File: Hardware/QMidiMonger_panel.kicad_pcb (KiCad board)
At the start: 2 copper layers, 40.3 x 128.5 mm, 26 parts

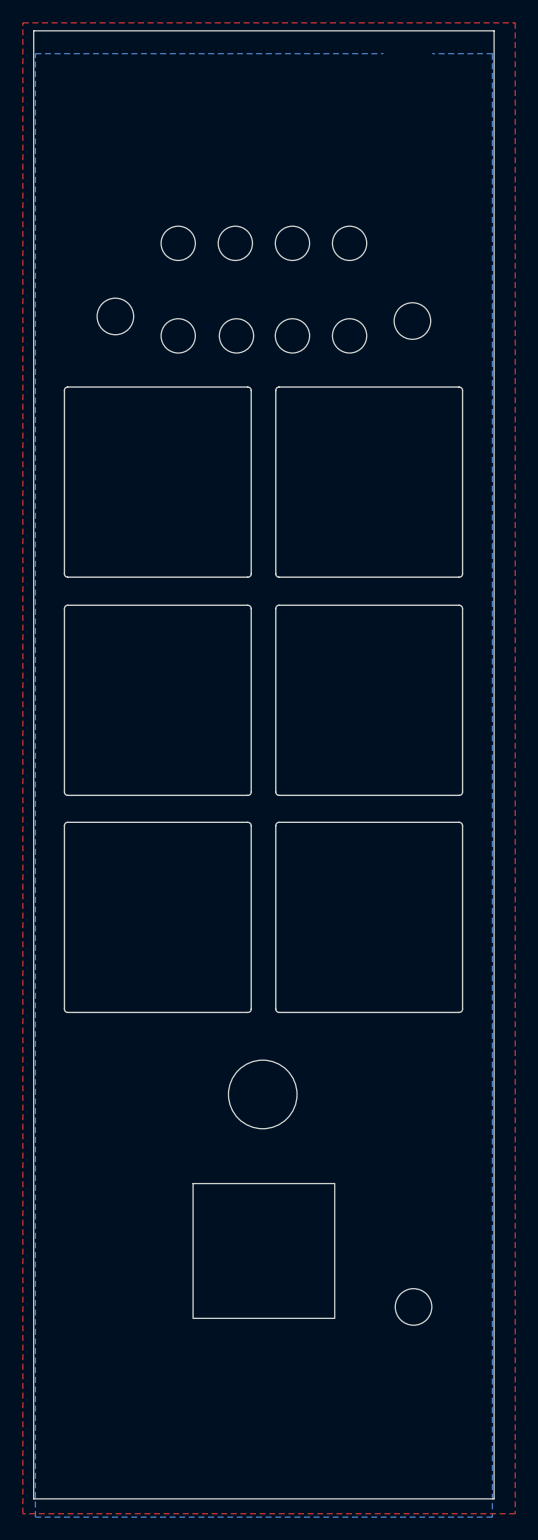
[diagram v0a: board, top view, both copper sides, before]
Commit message: Added inter-board connector
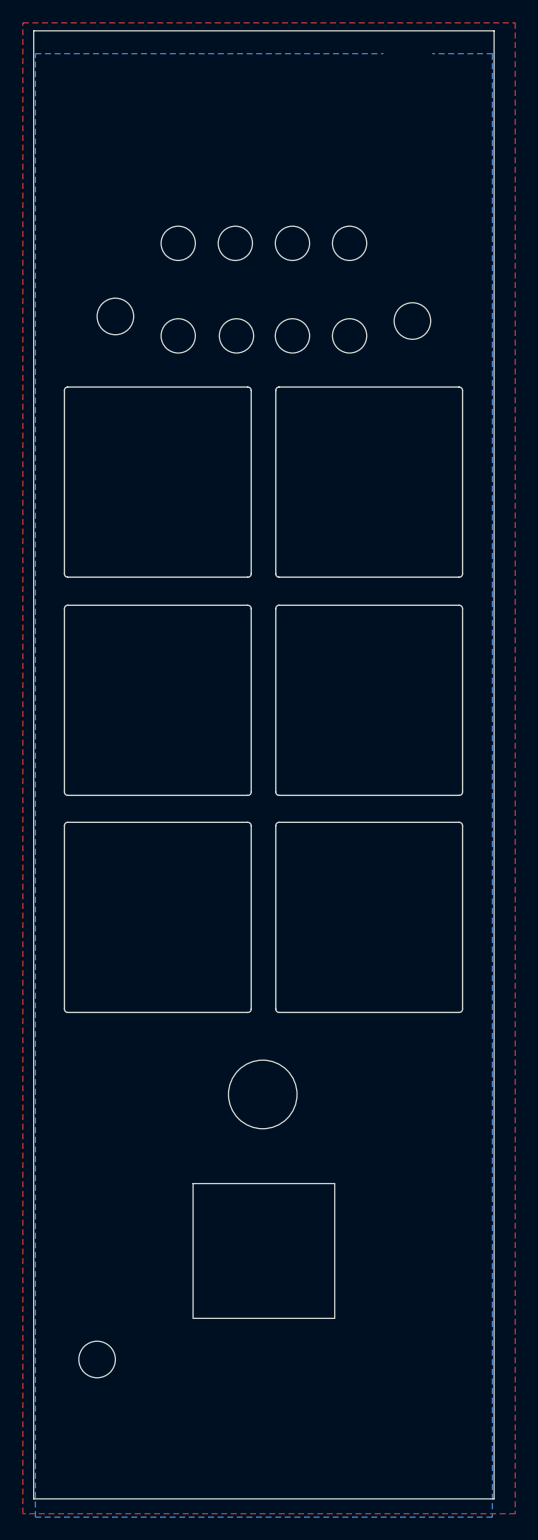
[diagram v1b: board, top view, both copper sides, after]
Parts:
- removed kibuzzard-63FE2BC1: G***, kibuzzard-63FE2BC1
- added kibuzzard-63FF48D8: G***, kibuzzard-63FF48D8, F.Cu at (116.0, 146.8)
- moved H3 28.1 mm to (101.4, 145.3)

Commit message: Cleaned up Panel and Controls
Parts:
- added H3: MountingHole, MountingHole:MountingHole_3.2mm_M3_ISO14580, F.Cu at (130.7, 142.4)
- moved H3 2.90 mm to (101.3, 142.4)
- moved Ref** 1.60 mm to (108.5, 54.1)
- moved Ref** 1.60 mm to (118.5, 54.1)
- moved Ref** 1.60 mm to (113.6, 54.1)
- moved Ref** 1.60 mm to (123.5, 54.1)
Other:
- board text added: "Mountjoy Modular 2023 Quad MIDI Monger Panel v1.0"
- board text removed: "Mountjoy Modular MIDI Monger Panel v1.0"
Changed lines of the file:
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@@
     (40 "Dwgs.User" user "User.Drawings")
     (41 "Cmts.User" user "User.Comments")
-    (42 "Eco1.User" user "User.Eco1")
-    (43 "Eco2.User" user "User.Eco2")
     (44 "Edge.Cuts" user)
     (45 "Margin" user)
@@
     )
     (pad_to_mask_clearance 0)
-    (grid_origin 96 40)
     (pcbplotparams
       (layerselection 0x00010fc_ffffffff)
@@
       (drillshape 0)
       (scaleselection 1)
-      (outputdirectory "Panel_PCB_Gerbers/")
+      (outputdirectory "Gerbers/QMidiMonger_Panel/")
     )
   )
@@
   )
   (footprint "Custom_Footprints:LED_Hole_3mm" (layer "F.Cu")
-    (at 108.5 55.7)
+    (at 108.5 54.1)
     (descr "Mounting Hole 6mm, no annular")
     (tags "mounting hole 6mm no annular")
@@
   )
   (footprint "Custom_Footprints:LED_Hole_3mm" (layer "F.Cu")
-    (at 118.5 55.7)
+    (at 118.5 54.1)
     (descr "Mounting Hole 6mm, no annular")
     (tags "mounting hole 6mm no annular")
@@
   )
   (footprint "Custom_Footprints:LED_Hole_3mm" (layer "F.Cu")
-    (at 113.6 55.7)
+    (at 113.6 54.1)
     (descr "Mounting Hole 6mm, no annular")
     (tags "mounting hole 6mm no annular")
@@
   )
   (footprint "Custom_Footprints:LED_Hole_3mm" (layer "F.Cu")
-    (at 123.5 55.7)
+    (at 123.5 54.1)
     (descr "Mounting Hole 6mm, no annular")
     (tags "mounting hole 6mm no annular")
@@
     (fp_line (start 7.88 -8.32) (end -7.88 -8.32) (layer "Edge.Cuts") (width 0.12))
     (fp_arc (start -7.88 8.32) (mid -8.081749 8.227632) (end -8.16 8.02) (layer "Edge.Cuts") (width 0.12))
-    (fp_arc (start 7.88 -8.32) (mid 8.096588 -8.233658) (end 8.19 -8.02) (layer "Edge.Cuts") (width 0.12))
+    (fp_arc (start 7.88 -8.32) (mid 8.096622 -8.233665) (end 8.19 -8.02) (layer "Edge.Cuts") (width 0.12))
     (fp_arc (start -8.16 -8.02) (mid -8.081443 -8.227347) (end -7.88 -8.32) (layer "Edge.Cuts") (width 0.12))
     (fp_arc (start 8.19 8.02) (mid 8.100917 8.238111) (end 7.88 8.32) (layer "Edge.Cuts") (width 0.12))
@@
     (fp_line (start -8.16 -8.02) (end -8.16 8.02) (layer "Edge.Cuts") (width 0.12))
     (fp_arc (start -8.16 -8.02) (mid -8.081443 -8.227347) (end -7.88 -8.32) (layer "Edge.Cuts") (width 0.12))
-    (fp_arc (start 7.88 -8.32) (mid 8.096588 -8.233658) (end 8.19 -8.02) (layer "Edge.Cuts") (width 0.12))
+    (fp_arc (start 7.88 -8.32) (mid 8.096622 -8.233665) (end 8.19 -8.02) (layer "Edge.Cuts") (width 0.12))
     (fp_arc (start 8.19 8.02) (mid 8.100917 8.238111) (end 7.88 8.32) (layer "Edge.Cuts") (width 0.12))
     (fp_arc (start -7.88 8.32) (mid -8.081749 8.227632) (end -8.16 8.02) (layer "Edge.Cuts") (width 0.12))
@@
     (fp_line (start 7.88 -8.32) (end -7.88 -8.32) (layer "Edge.Cuts") (width 0.12))
     (fp_arc (start 8.19 8.02) (mid 8.100917 8.238111) (end 7.88 8.32) (layer "Edge.Cuts") (width 0.12))
-    (fp_arc (start 7.88 -8.32) (mid 8.096588 -8.233658) (end 8.19 -8.02) (layer "Edge.Cuts") (width 0.12))
+    (fp_arc (start 7.88 -8.32) (mid 8.096622 -8.233665) (end 8.19 -8.02) (layer "Edge.Cuts") (width 0.12))
     (fp_arc (start -7.88 8.32) (mid -8.081749 8.227632) (end -8.16 8.02) (layer "Edge.Cuts") (width 0.12))
     (fp_arc (start -8.16 -8.02) (mid -8.081443 -8.227347) (end -7.88 -8.32) (layer "Edge.Cuts") (width 0.12))
@@
     (attr board_only exclude_from_pos_files exclude_from_bom)
     (fp_text reference "kibuzzard-63FF48D8" (at 0 -5.016252) (layer "F.SilkS") hide
-      (effects (font (size 0 0)))
+      (effects (font (size 0 0) (thickness 0.15)))
     )
     (fp_text value "G***" (at 0 5.016252) (layer "F.SilkS") hide
-      (effects (font (size 0 0)))
+      (effects (font (size 0 0) (thickness 0.15)))
     )
     (fp_poly (pts
@@
     (fp_arc (start -7.88 8.32) (mid -8.081749 8.227632) (end -8.16 8.02) (layer "Edge.Cuts") (width 0.12))
     (fp_arc (start 8.19 8.02) (mid 8.100917 8.238111) (end 7.88 8.32) (layer "Edge.Cuts") (width 0.12))
-    (fp_arc (start 7.88 -8.32) (mid 8.096588 -8.233658) (end 8.19 -8.02) (layer "Edge.Cuts") (width 0.12))
+    (fp_arc (start 7.88 -8.32) (mid 8.096622 -8.233665) (end 8.19 -8.02) (layer "Edge.Cuts") (width 0.12))
     (fp_arc (start -8.16 -8.02) (mid -8.081443 -8.227347) (end -7.88 -8.32) (layer "Edge.Cuts") (width 0.12))
     (fp_line (start -8.31 8.5) (end 8.39 8.5) (layer "F.CrtYd") (width 0.05))
@@
     (fp_arc (start 8.19 8.02) (mid 8.100917 8.238111) (end 7.88 8.32) (layer "Edge.Cuts") (width 0.12))
     (fp_arc (start -8.16 -8.02) (mid -8.081443 -8.227347) (end -7.88 -8.32) (layer "Edge.Cuts") (width 0.12))
-    (fp_arc (start 7.88 -8.32) (mid 8.096588 -8.233658) (end 8.19 -8.02) (layer "Edge.Cuts") (width 0.12))
+    (fp_arc (start 7.88 -8.32) (mid 8.096622 -8.233665) (end 8.19 -8.02) (layer "Edge.Cuts") (width 0.12))
     (fp_arc (start -7.88 8.32) (mid -8.081749 8.227632) (end -8.16 8.02) (layer "Edge.Cuts") (width 0.12))
     (fp_line (start -8.31 -8.5) (end -8.31 8.5) (layer "F.CrtYd") (width 0.05))
@@
   )
   (footprint "MountingHole:MountingHole_3.2mm_M3_ISO14580" (layer "F.Cu")
-    (at 101.4 145.3)
+    (at 101.3 142.4)
     (descr "Mounting Hole 3.2mm, no annular, M3, ISO14580")
     (tags "mounting hole 3.2mm no annular m3 iso14580")
@@
       ) (layer "F.Mask") (width 0) (fill solid))
   )
+  (footprint "MountingHole:MountingHole_3.2mm_M3_ISO14580" (layer "F.Cu")
+    (at 130.7 142.4)
+    (descr "Mounting Hole 3.2mm, no annular, M3, ISO14580")
+    (tags "mounting hole 3.2mm no annular m3 iso14580")
+    (property "Sheetfile" "D:/Eurorack/MidiMonger/Hardware/QMidiMonger_controls.sch")
+    (property "Sheetname" "")
+    (attr exclude_from_pos_files)
+    (fp_text reference "H3" (at 0 -3.75) (layer "F.SilkS") hide
+      (effects (font (size 1 1) (thickness 0.15)))
+    )
+    (fp_text value "MountingHole" (at 0 3.75) (layer "F.Fab")
+      (effects (font (size 1 1) (thickness 0.15)))
+    )
+    (fp_text user "${REFERENCE}" (at 0 0) (layer "F.Fab")
+      (effects (font (size 1 1) (thickness 0.15)))
+    )
+    (fp_circle (center 0 0) (end 2.75 0) (layer "Cmts.User") (width 0.15) (fill none))
+    (fp_circle (center 0 0) (end 3 0) (layer "F.CrtYd") (width 0.05) (fill none))
+    (pad "" np_thru_hole circle (at 0 0) (size 3.2 3.2) (drill 3.2) (layers F&B.Cu *.Mask))
+  )
   (footprint "Custom_Footprints:RJ45_Molex_42878-8506_Mounting_Hole" (layer "F.Cu")
     (at 106.7 106.6)
@@
     (fp_arc (start -7.88 8.32) (mid -8.081749 8.227632) (end -8.16 8.02) (layer "Edge.Cuts") (width 0.12))
     (fp_arc (start 8.19 8.02) (mid 8.100917 8.238111) (end 7.88 8.32) (layer "Edge.Cuts") (width 0.12))
-    (fp_arc (start 7.88 -8.32) (mid 8.096588 -8.233658) (end 8.19 -8.02) (layer "Edge.Cuts") (width 0.12))
+    (fp_arc (start 7.88 -8.32) (mid 8.096622 -8.233665) (end 8.19 -8.02) (layer "Edge.Cuts") (width 0.12))
     (fp_line (start -8.31 8.5) (end 8.39 8.5) (layer "F.CrtYd") (width 0.05))
     (fp_line (start 8.39 -8.5) (end 8.39 8.5) (layer "F.CrtYd") (width 0.05))
@@
     (effects (font (size 1 1) (thickness 0.15)) (justify mirror))
   )
-  (gr_text "Mountjoy Modular\nMIDI Monger Panel v1.0" (at 116.2 33.8) (layer "B.SilkS")
+  (gr_text "Mountjoy Modular 2023\nQuad MIDI Monger Panel v1.0" (at 116.2 41.5) (layer "B.SilkS")
     (effects (font (size 1 1) (thickness 0.15)) (justify mirror))
   )
@@
     (effects (font (size 1.5 1.5) (thickness 0.3)))
   )
-  (zone (net 0) (net_name "") (layer "F.Cu") (hatch edge 0.508)
+  (zone (net 0) (net_name "") (layers F&B.Cu) (hatch edge 0.508)
     (connect_pads (clearance 0.508))
     (min_thickness 0.254) (filled_areas_thickness no)
@@
       )
     )
-  )
-  (zone (net 0) (net_name "") (layer "B.Cu") (hatch edge 0.508)
-    (connect_pads (clearance 0.508))
-    (min_thickness 0.254) (filled_areas_thickness no)
-    (fill yes (thermal_gap 0.508) (thermal_bridge_width 0.508))
-    (polygon
-      (pts
-        (xy 96 31)
-        (xy 136 31)
-        (xy 136 159.1)
-        (xy 96 159.1)
-      )
-    )
